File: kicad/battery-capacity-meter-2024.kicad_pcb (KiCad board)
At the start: 4 copper layers, 100 x 123.9 mm, 57 parts, among them J1 PWR, J2 GND, J3 Conn_MainBoard, J4 Conn_DisplayBoard, Q1 2N3904, Q2 2N3906, Q3 2SD2390, SW1 SW_CHARGE/DISCHARGE, SW2 1A MODE, U1 LM2596_StepDown_Module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

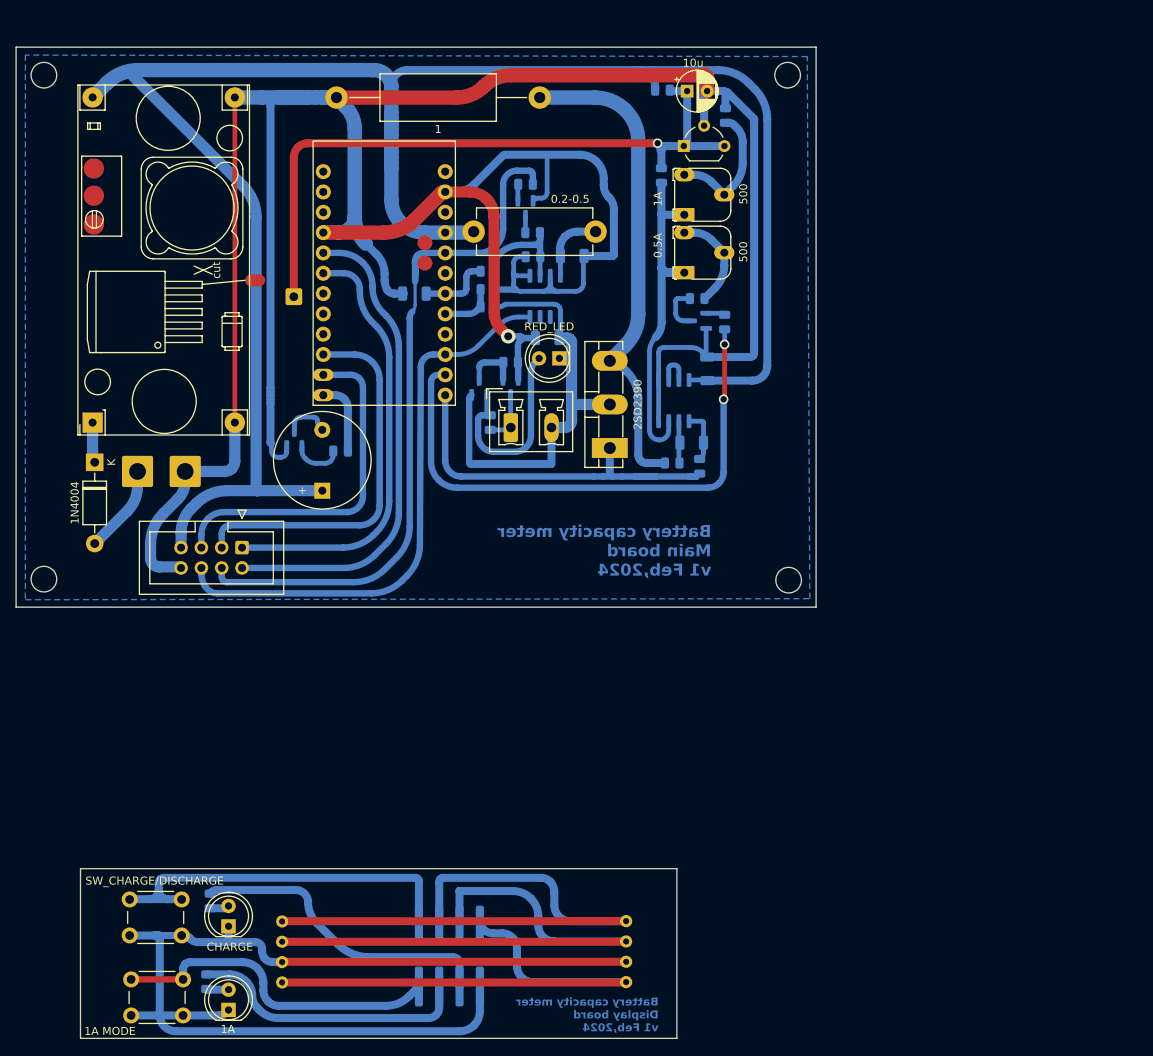
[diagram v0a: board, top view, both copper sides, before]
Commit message: hardware-ok. firware barelly workin
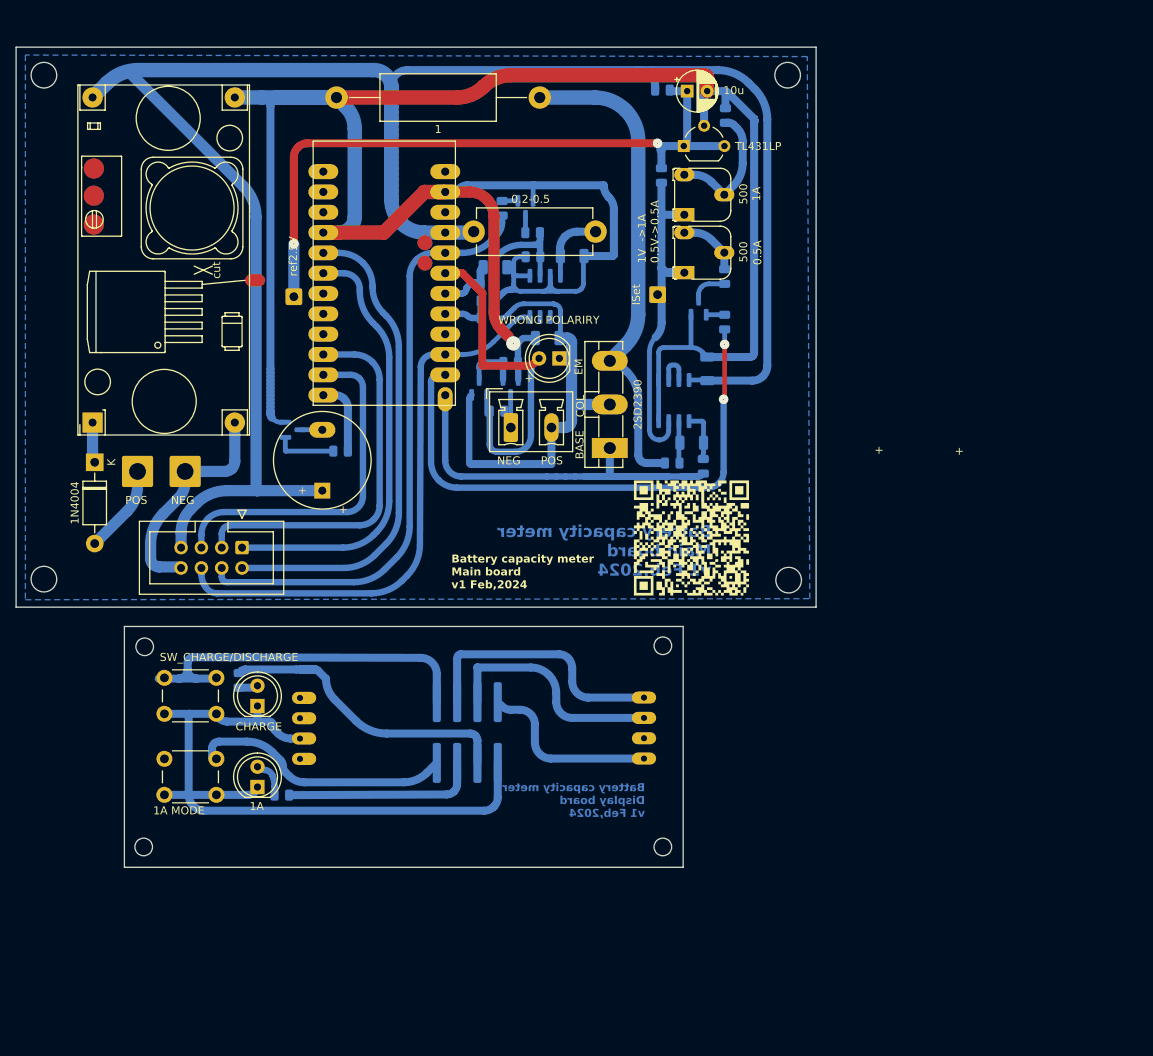
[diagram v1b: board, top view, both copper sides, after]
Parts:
- added G***: LOGO, LOGO, F.Cu at (173.5, 113.2)
- added H5: MountingHole, MountingHole:MountingHole_2.2mm_M2, F.Cu at (169.8, 151.7)
- added H6: MountingHole, MountingHole:MountingHole_2.2mm_M2, F.Cu at (169.8, 126.6)
- added H7: MountingHole, MountingHole:MountingHole_2.2mm_M2, F.Cu at (104.9, 151.7)
- added H8: MountingHole, MountingHole:MountingHole_2.2mm_M2, F.Cu at (105.1, 126.7)
- added TP1: ISet, Connector_Wire:SolderWire-0.5sqmm_1x01_D0.9mm_OD2.1mm, F.Cu at (169.2, 82.7)
- D2: value RED_LED -> WRONG POLARIRY
- moved D4 28.1 mm to (119.2, 144.2)
- moved SW1 28.0 mm to (107.5, 130.6)
- moved J4 28.0 mm to (145.4, 137.4)
- moved U3 28.0 mm to (144.0, 135.1)
- moved SW2 27.9 mm to (107.5, 140.7)
- moved R19 27.8 mm to (116.9, 130.9)
- moved D3 27.8 mm to (119.2, 134.1)
- moved R20 25.1 mm to (122.2, 145.2), turned to 180 degrees
- moved C5 10.6 mm to (148.8, 79.2), turned to 0 degrees
- moved R17 4.39 mm to (177.5, 80.4), turned to -90 degrees
- moved R18 4.19 mm to (149.7, 71.9), turned to -90 degrees
- moved U9 1.71 mm to (174.3, 84.2), turned to 90 degrees
- moved R8 1.66 mm to (149.1, 97.2), turned to 180 degrees
- moved R2 1.65 mm to (148.0, 81.4)
- moved R6 1.40 mm to (148.0, 85.6)
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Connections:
- net BTN_0.5A_MODE renamed BTN_1A_MODE
- D2 pad 2: Net-(D2-A) -> POLARITY_SENSE
- Q2 pad 1: Net-(D2-A) -> POLARITY_SENSE
- R8 pad 2: Net-(D2-A) -> POLARITY_SENSE
- U7 pad A2: unconnected-(U7-PadA2) -> POLARITY_SENSE
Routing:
- net GND: track 534.6 -> 418.7 mm
- net POLARITY_SENSE: track 0.00 -> 45.5 mm
- net +5V: track 310.7 -> 267.8 mm
- net DIO: track 115.9 -> 72.9 mm
- net CLK: track 123.6 -> 80.7 mm
- net Net-(D2-A): track 24.7 -> 0.00 mm
- net 1A_MODE: track 122.2 -> 100.1 mm
- net BTN_1A_MODE: track 103.0 -> 93.8 mm
- net Net-(R17-Pad1): track 12.5 -> 7.52 mm
- net Net-(Battery1-Pin_1): track 6.83 -> 4.05 mm
- net Net-(BZ1-+): track 5.39 -> 2.75 mm
- net BTN_CHARGE_DISCHARGE: track 104.3 -> 101.7 mm
- net Net-(D4-A): track 2.69 -> 4.63 mm
- net CHRG_EN: track 109.8 -> 108.1 mm
- net I_SENSE: track 9.03 -> 7.36 mm
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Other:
- board size 100 x 123.9 mm -> 100 x 102.5 mm
- board text added: "+"
- board text added: "1V ->1A 0.5V->0.5A"
- board text added: "BASE"
- board text added: "COL"
- board text added: "EM"
- board text added: "NEG"
- board text added: "POS"
- board text added: "ref2.5V"

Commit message: working v1
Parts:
- added R21: 10k, Resistor_SMD:R_0805_2012Metric, B.Cu at (139.2, 80.9)
- R19: value 10k -> 3k
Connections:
- D2 pad 2: POLARITY_SENSE -> Net-(D2-A)
- Q2 pad 1: POLARITY_SENSE -> Net-(D2-A)
- R8 pad 2: POLARITY_SENSE -> Net-(D2-A)
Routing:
- net POLARITY_SENSE: track 45.5 -> 2.96 mm
- net Net-(Battery1-Pin_1): track 4.05 -> 32.1 mm, vias 0 -> 1
- net Net-(D2-A): track 0.00 -> 23.3 mm
- net 1A_MODE: track 100.1 -> 105.6 mm

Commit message: add ovp
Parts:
- removed D2: WRONG POLARIRY, LED_THT:LED_D5.0mm
- added C1: 47n, Capacitor_SMD:C_1206_3216Metric, B.Cu at (198.2, 91.9)
- added D5: 1N4734A 5.6V, Diode_THT:D_DO-35_SOD27_P5.08mm_Vertical_KathodeUp, F.Cu at (205.6, 91.4)
- added F1: 2A, Resistor_THT:R_Axial_DIN0309_L9.0mm_D3.2mm_P2.54mm_Vertical, F.Cu at (206.0, 88.2)
- added Q6: X0402MF, Package_TO_SOT_THT:TO-220-3_Vertical, F.Cu at (200.5, 89.4)
- moved R21 57.8 mm to (195.9, 92.1)
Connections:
- C6 pad 1: Net-(Battery1-Pin_2) -> Net-(D5-K)
- Q2 pad 2: Net-(Battery1-Pin_2) -> Net-(D5-K)
- Q3 pad 2: Net-(Battery1-Pin_2) -> Net-(D5-K)
- R21 pad 1: Net-(Battery1-Pin_1) -> POLARITY_SENSE
- R21 pad 2: POLARITY_SENSE -> Net-(Battery1-Pin_1)
- R6 pad 1: Net-(Battery1-Pin_2) -> Net-(D5-K)
- U8 pad 5: Net-(Battery1-Pin_2) -> Net-(D5-K)
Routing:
- net Net-(D5-K): track 0.00 -> 90.1 mm
- net Net-(Battery1-Pin_2): track 56.0 -> 12.4 mm
- net Net-(Battery1-Pin_1): track 32.1 -> 10.9 mm, vias 1 -> 0
- net Net-(Q2-B): track 23.3 -> 2.43 mm
- net POLARITY_SENSE: track 2.96 -> 16.6 mm
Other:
- board text added: "A2"
- board text added: "Battery capacity meter Main board v2 Feb,2024"
- board text added: "bat+"
- board text added: "bat-"
- board text added: "to TP5046"

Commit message: add overvoltage protection in hardware and cycle modes in firmware
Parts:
- removed F1: 2A, Resistor_THT:R_Axial_DIN0309_L9.0mm_D3.2mm_P2.54mm_Vertical
- added D2: 1N4148, Diode_SMD:D_MiniMELF, B.Cu at (155.8, 92.8)
- added D6: 1N4148, Diode_SMD:D_MiniMELF, B.Cu at (207.9, 85.7)
- added D7: BAT54S, Package_TO_SOT_SMD:SOT-23, B.Cu at (195.4, 87.9)
- added D9: BAT54S, Package_TO_SOT_SMD:SOT-23, B.Cu at (195.2, 93.1)
- added R22: 10k, Resistor_SMD:R_0805_2012Metric, B.Cu at (198.3, 94.1)
- added R23: 0.1, Resistor_SMD:R_2512_6332Metric, B.Cu at (201.6, 92.4)
- added R24: 10k, Resistor_SMD:R_0805_2012Metric, B.Cu at (198.4, 86.9)
- added R25: 10k, Resistor_SMD:R_0805_2012Metric, B.Cu at (198.8, 98.0)
- added R26: 470, Resistor_SMD:R_0805_2012Metric, B.Cu at (196.0, 97.0)
- added TH1: 1A, !my-lib:PTC_1A_radial, F.Cu at (209.5, 83.3)
- added TH2: 1A, !my-lib:PTC_1A_radial, F.Cu at (215.8, 83.3)
- Battery1: footprint Connector_Phoenix_MC_HighVoltage:PhoenixContact_MCV_1,5_2-G-5.08_1x02_P5.08mm_Vertical -> Connector_JST:JST_VH_B2P-VH-B_1x02_P3.96mm_Vertical
- C1: value 47n -> 10n
- D5: value 1N4734A 5.6V -> 1N4732A 4.7V; footprint Diode_THT:D_DO-35_SOD27_P5.08mm_Vertical_KathodeUp -> Diode_SMD:D_MiniMELF; moved to B.Cu
- moved Battery1 58.5 mm to (209.3, 98.5)
- moved R21 12.0 mm to (207.9, 92.1), turned to -90 degrees
- moved Q6 11.4 mm to (203.0, 78.2)
- moved D5 11.2 mm to (212.1, 82.3)
- moved C1 7.14 mm to (205.4, 92.2), turned to -90 degrees
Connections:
- C1 pad 1: POLARITY_SENSE -> Net-(D6-K)
- D5 pad 2: POLARITY_SENSE -> Net-(D5-A)
- Q6 pad 1: Net-(Battery1-Pin_1) -> Net-(Q6-K)
- Q6 pad 3: POLARITY_SENSE -> Net-(D6-K)
- R21 pad 1: POLARITY_SENSE -> Net-(D6-K)
- U2 pad 5: GND -> Net-(D7-COM)
- U2 pad 7: Net-(U2B--) -> OVP_SENSE
- U7 pad 4: unconnected-(U7-Pad4) -> OVP_SENSE
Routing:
- net Net-(Battery1-Pin_1): track 10.9 -> 106.7 mm, vias 0 -> 2
- net OVP_SENSE: track 0.00 -> 87.5 mm, vias 0 -> 1
- net POLARITY_SENSE: track 16.6 -> 98.3 mm, vias 0 -> 1
- net 2.5Vref: track 84.3 -> 149.1 mm, vias 2 -> 3
- net Net-(D7-COM): track 0.00 -> 38.9 mm, vias 0 -> 2
- net Net-(U2B--): track 4.58 -> 38.8 mm, vias 0 -> 2
- net Net-(D2-K): track 90.1 -> 120.8 mm
- net GND: track 418.7 -> 449.1 mm, vias 1 -> 4
- net Net-(D2-A): track 2.43 -> 22.2 mm
- net +5V: track 267.8 -> 287.1 mm, vias 0 -> 2
- net Net-(Q6-K): track 0.00 -> 18.1 mm
- net Net-(D6-K): track 0.00 -> 12.7 mm
- net Net-(D5-A): track 0.00 -> 3.71 mm
- net Net-(Battery1-Pin_2): track 12.4 -> 16.0 mm
- net Net-(Q3-E): track 60.6 -> 59.4 mm
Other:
- board size 100 x 102.5 mm -> 140.1 x 102.5 mm
- board text added: "2.5Vref"
- board text added: "5V"
- board text added: "GND"
- board text added: "oldBat+"
- board text added: "oldBat-"
- board text added: "opAmp5"
- board text added: "opAmp6"
- board text removed: "Battery capacity meter Main board v1 Feb,2024"
- board text removed: "to TP5046"

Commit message: before tracks reset
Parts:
- removed J1: PWR, Connector_Wire:SolderWire-1.5sqmm_1x01_D1.7mm_OD3.9mm
- removed J2: GND, Connector_Wire:SolderWire-1.5sqmm_1x01_D1.7mm_OD3.9mm
- added J5: PWR, Connector_JST:JST_XH_B2B-XH-A_1x02_P2.50mm_Vertical, F.Cu at (105.7, 104.6)
- added R27: 1M, Resistor_SMD:R_0805_2012Metric, B.Cu at (162.6, 86.0)
- R26: value 470 -> 150
- SW1: value SW_CHARGE/DISCHARGE -> CHARGE/DISCHARGE
- moved R12 4.88 mm to (124.2, 58.1)
- moved D3 0.05 mm to (119.2, 134.0)
- moved D4 0.05 mm to (119.2, 144.2)
- moved H5 0.05 mm to (169.8, 151.7)
- moved H7 0.05 mm to (104.9, 151.7)
- moved J4 0.05 mm to (145.4, 137.4), turned to 90 degrees
- moved SW1 0.05 mm to (107.5, 130.5)
- moved U3 0.05 mm to (144.0, 135.1)
- moved AREF1 0.05 mm to (123.7, 82.9)
- moved BZ1 0.05 mm to (127.3, 107.1)
- moved Battery1 0.05 mm to (209.3, 98.5)
- moved C1 0.05 mm to (205.4, 92.1)
- moved C4 0.05 mm to (158.5, 77.8)
- moved C5 0.05 mm to (148.8, 79.2)
- moved C6 0.05 mm to (155.4, 88.1)
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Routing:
- net BTN_1A_MODE: track 93.8 -> 140.7 mm, vias 0 -> 1
- net BTN_CHARGE_DISCHARGE: track 101.7 -> 131.5 mm, vias 0 -> 1
- net DIO: track 72.9 -> 88.6 mm
- net 1A_MODE: track 105.6 -> 120.9 mm, vias 0 -> 2
- net GND: track 449.1 -> 434.2 mm
- net CLK: track 80.7 -> 74.0 mm
- net CHRG_EN: track 108.1 -> 102.3 mm
- net +5V: track 287.1 -> 281.5 mm
- net Net-(Q3-E): track 59.4 -> 64.3 mm
- net Net-(D1-A): track 11.0 -> 12.6 mm
- net 2.5Vref: vias 3 -> 2
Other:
- board text added: "1A MODE"
- board text added: "BTN_1A_MODE"
- board text added: "Battery capacity meter Display board v3 Feb,2024"
- board text added: "Battery capacity meter Main board v3 Feb,2024"
- board text added: "CHRG_EN"
- board text added: "CLK"
- board text added: "DIO"
- board text removed: "Battery capacity meter Display board v1 Feb,2024"

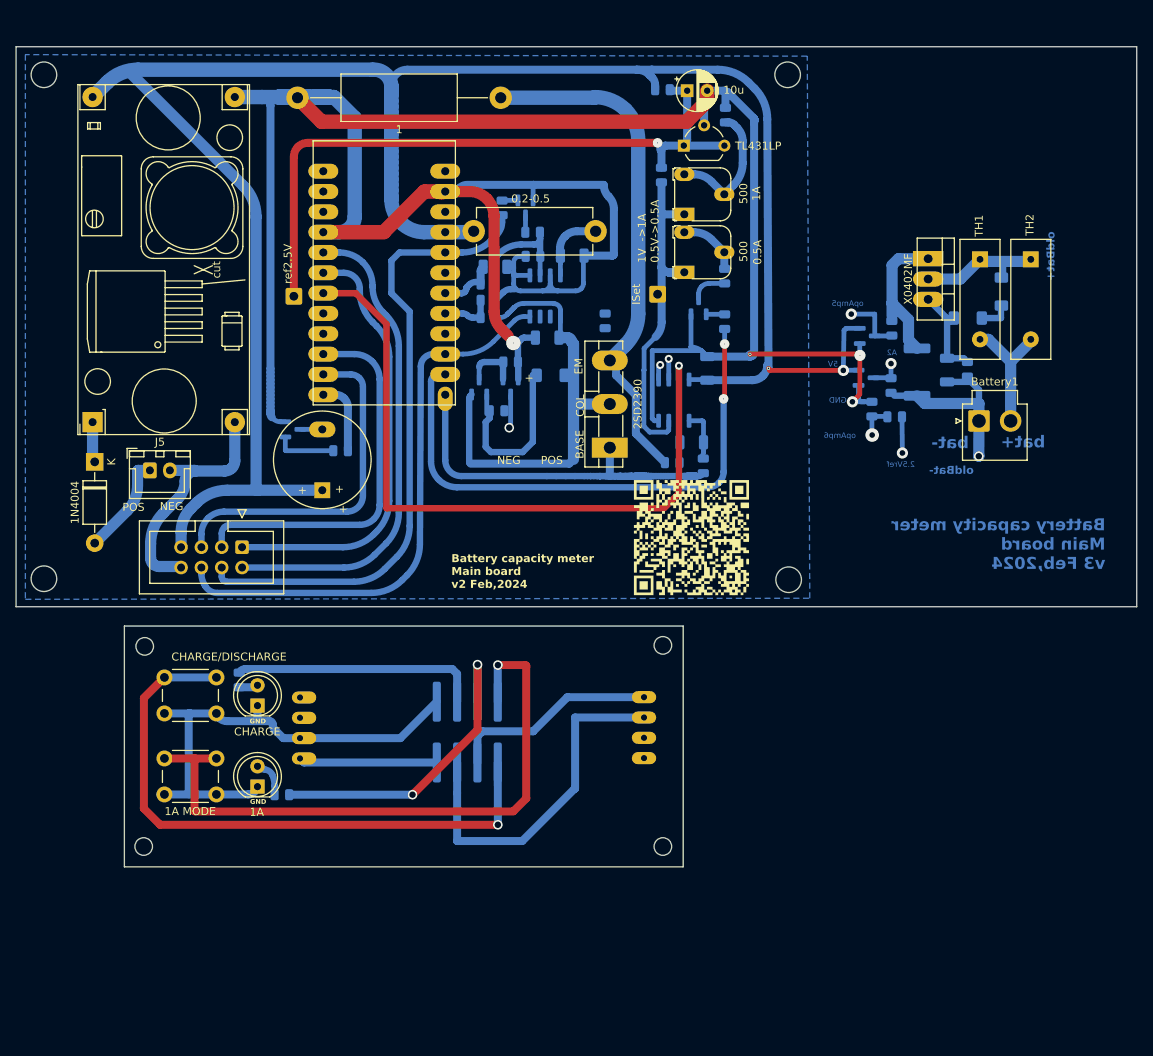
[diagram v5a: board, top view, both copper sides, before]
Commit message: ready two layers
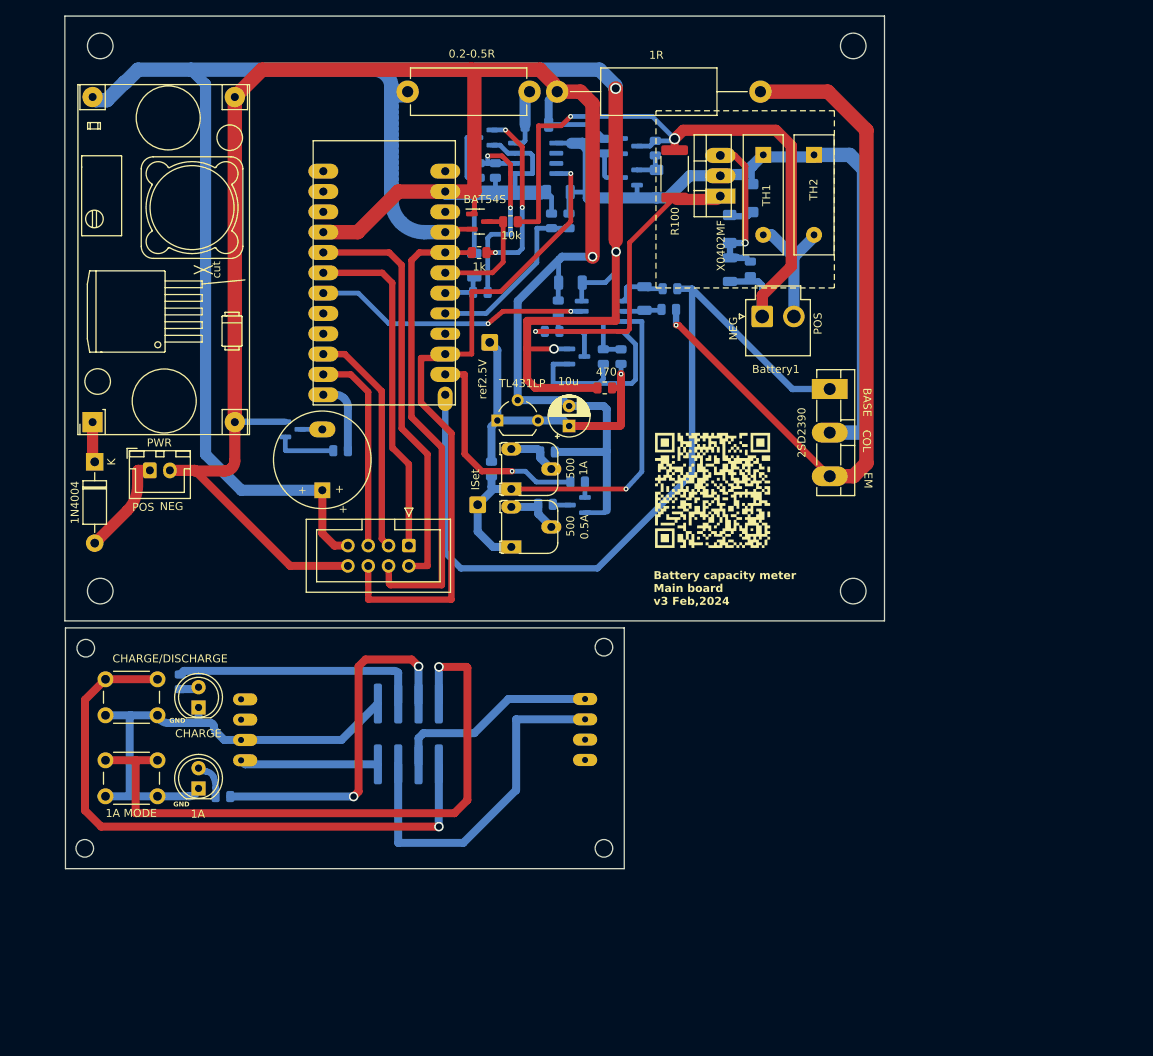
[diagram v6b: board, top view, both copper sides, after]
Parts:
- D9, R13, R18, R22: moved to F.Cu
- R1: value 0.2-0.5 -> 0.2-0.5R
- R12: value 1 -> 1R
- R23: value 0.1 -> R100; moved to F.Cu
- R26: value 150 -> 150R
- moved D9 52.1 mm to (146.9, 73.5)
- moved R22 51.8 mm to (150.8, 73.6), turned to 180 degrees
- moved R15 47.6 mm to (155.4, 102.3), turned to 0 degrees
- moved C9 44.4 mm to (158.1, 99.1), turned to 90 degrees
- moved R24 42.5 mm to (156.0, 87.3), turned to 0 degrees
- moved R14 42.4 mm to (148.4, 104.5)
- moved U6 41.5 mm to (149.1, 98.4)
- moved RV1 40.6 mm to (150.9, 107.0)
- moved RV2 40.6 mm to (150.9, 114.2)
- moved R23 39.1 mm to (171.3, 67.6), turned to 90 degrees
- moved R8 38.3 mm to (168.9, 64.4), turned to -90 degrees
- moved R13 38.0 mm to (162.6, 94.3)
- moved D7 36.4 mm to (159.1, 90.4)
- moved R17 36.3 mm to (155.2, 108.9), turned to 0 degrees
- moved R25 35.0 mm to (164.6, 90.4), turned to 90 degrees
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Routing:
- net 2.5Vref: track 149.1 -> 40.2 mm, vias 2 -> 1
- net POLARITY_SENSE: track 98.3 -> 14.9 mm, vias 1 -> 0
- net DSCHRG_EN: track 45.0 -> 103.7 mm
- net OVP_SENSE: track 87.5 -> 34.4 mm, vias 1 -> 2
- net GND: track 434.2 -> 389.1 mm, vias 4 -> 1
- net !1A_MODE: track 69.6 -> 27.0 mm, vias 2 -> 1
- net Net-(D7-COM): track 38.9 -> 7.89 mm, vias 2 -> 0
- net Net-(U2B--): track 38.8 -> 8.29 mm, vias 2 -> 0
- net Net-(D2-K): track 120.8 -> 93.8 mm
- net Net-(Q3-E): track 64.3 -> 91.1 mm, vias 0 -> 1
- net Net-(Battery1-Pin_1): track 106.7 -> 86.5 mm
- net Net-(U10-G): track 1.98 -> 22.0 mm, vias 0 -> 3
- net CLK: track 74.0 -> 55.0 mm
- net Net-(Q6-K): track 18.1 -> 36.8 mm, vias 0 -> 1
- net Net-(D2-A): track 22.2 -> 4.10 mm
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- removed copper zone on B.Cu, net GND
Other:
- board size 140.1 x 102.5 mm -> 102.5 x 106.6 mm
- copper layers 4 -> 2
- board text added: "BTN_CHRG_DISCHRG"
- board text removed: "1V ->1A 0.5V->0.5A"
- board text removed: "2.5Vref"
- board text removed: "A2"
- board text removed: "Battery capacity meter Main board v2 Feb,2024"
- board text removed: "oldBat+"
- board text removed: "oldBat-"
- board text removed: "opAmp5"
- board text removed: "opAmp6"

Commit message: jlc-pcb order
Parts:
- moved H5 8.23 mm to (167.2, 145.1)
- moved H7 6.77 mm to (98.1, 145.1)
- moved G*** 5.80 mm to (176.1, 101.4)
- moved H6 4.82 mm to (167.2, 125.7)
- moved D3 4.37 mm to (115.2, 131.6)
- moved J4 4.37 mm to (141.5, 134.9)
- moved D4 4.37 mm to (115.2, 141.7)
- moved R19 4.37 mm to (113.0, 128.4)
- moved R20 4.37 mm to (118.3, 142.8)
- moved U3 4.37 mm to (140.1, 132.6)
- moved SW1 4.37 mm to (103.6, 128.1)
- moved SW2 4.37 mm to (103.6, 138.2)
- moved Q3 1.78 mm to (188.9, 94.4)
- moved H2 1.70 mm to (192.2, 118.8)
- moved H1 1.46 mm to (192.2, 51.6)
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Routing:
- net DIO: track 70.5 -> 56.9 mm, vias 0 -> 1
- net DSCHRG_EN: track 103.7 -> 96.7 mm
- net Net-(D1-A): track 12.6 -> 15.5 mm
- net 1A_MODE: track 103.8 -> 102.2 mm
- net CHRG_EN: track 115.2 -> 113.8 mm
- net Net-(D2-K): track 93.8 -> 92.6 mm
- net Net-(Q3-E): track 91.1 -> 91.7 mm
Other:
- board size 102.5 x 106.6 mm -> 100 x 99.9 mm
